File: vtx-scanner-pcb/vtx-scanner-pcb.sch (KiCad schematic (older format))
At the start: 15 parts, among them U1 RX5808, U3 oskj-dc-dc

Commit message: Lots of progress with the schematic and a bit of the PCB
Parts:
- added J2: Conn_01x08_Female, Connector_PinHeader_2.54mm:PinHeader_1x08_P2.54mm_Horizontal, symbol Connector:Conn_01x08_Female
- added R4, R5, R6, R7: 10K, Resistor_SMD:R_1206_3216Metric_Pad1.42x1.75mm_HandSolder, symbol Device:R
- added S1, S2, S3, S4: B3F-1000, digikey-footprints:Switch_Tactile_THT_B3F-1xxx, symbol dk_Tactile-Switches:B3F-1000
- A1: renamed from A?; footprint XCVR_ESP32-WROVER-I -> deets:XCVR_ESP32-WROVER-I
- C1, C2: renamed from C?; footprint (none) -> Capacitor_SMD:CP_Elec_5x5.8
- C3: renamed from C?; footprint (none) -> Capacitor_SMD:C_0805_2012Metric_Pad1.15x1.40mm_HandSolder
- J1: renamed from J?; footprint (none) -> Connector_PinHeader_2.54mm:PinHeader_1x06_P2.54mm_Vertical
- R1, R2: renamed from R?; value 12K -> 10K; footprint (none) -> Resistor_SMD:R_1206_3216Metric_Pad1.42x1.75mm_HandSolder
- R3: renamed from R?; footprint (none) -> Resistor_SMD:R_1206_3216Metric_Pad1.42x1.75mm_HandSolder
- U1: footprint vtx-scanner:RX5808 -> deets:RX5808
- U3: footprint new-joy:oskj-dc-dc -> deets:oskj-dc-dc
- U4: renamed from U?; footprint (none) -> deets:AI-1027-TWT
- gave numbers to parts that had none: 4
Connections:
- net labels added: BUTTON_DOWN, BUTTON_LEFT, BUTTON_RIGHT, BUTTON_UP, SSD1306_CLK, SSD1306_CS, SSD1306_DATA, SSD1306_DC, SSD1306_RST, VRX_CLOCK, VRX_CS, VRX_DATA, VRX_RSSI
- net labels removed: +3V3
- wire segments 33 -> 63
- no-connect marks 6 -> 20
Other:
- note added: "strapping pin\n"
- moved on the sheet: C3, U1

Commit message: Started laying out PCB
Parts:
- removed Q1, Q2, Q3: S8050, Package_TO_SOT_THT:TO-92_Inline, symbol Transistor_BJT:S8050
- removed S1, S2, S3, S4: B3F-1000, digikey-footprints:Switch_Tactile_THT_B3F-1xxx, symbol dk_Tactile-Switches:B3F-1000
- added J3: SMA-J-P-H-RA-TH1, deets:SAMTEC_SMA-J-P-H-RA-TH1, symbol deets:SMA-J-P-H-RA-TH1
- added Q1, Q2, Q3: MMSS8050-H-TP, digikey-footprints:SOT-23-3, symbol dk_Transistors-Bipolar-BJT-Single:MMSS8050-H-TP
- added S1, S2, S3, S4: FSM4JSMATR, deets:Switch_Tactile_SMD_6x6mm, symbol dk_Tactile-Switches:FSM4JSMATR
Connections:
- net labels added: ANT, GNDA
- wire segments 63 -> 64
- no-connect marks 20 -> 19
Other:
- moved on the sheet: R4

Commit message: Fully laid-out 4 layer PCB, the first!
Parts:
- added J4: Conn_01x05, Connector_JST:JST_PH_S5B-PH-K_1x05_P2.00mm_Horizontal, symbol Connector_Generic:Conn_01x05
- added J5: XT60-M, deets:AMASS_XT60-M-SIDE-MOUNT, symbol deets:XT60-M
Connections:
- net +3V3: now also J4.2 (Pin_2)
- net +5V: now also J4.1 (Pin_1)
- net +BATT: now also J5.2 (+)
- net -BATT: now also J3.2 (GND), J3.3 (GND), J3.4 (GND), J3.5 (GND), U1.1 (AGND), U1.3 (AGND), J4.5 (Pin_5), J5.1 (-)
- net GNDA: no longer J3.2 (GND), J3.3 (GND), J3.4 (GND), J3.5 (GND), U1.1 (AGND), U1.3 (AGND)
- net EXP1: now reaches A1.26 (IO4)
- net EXP1: now also J4.3 (Pin_3)
- net EXP2: now reaches A1.7 (IO35)
- net EXP2: now also J4.4 (Pin_4)
- no-connect marks 19 -> 17
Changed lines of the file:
@@
 Text Label 6200 4400 0    50   ~ 0
 BUTTON_DOWN
-NoConn ~ 5000 3300
-NoConn ~ 6200 3900
 NoConn ~ 6200 4700
 Text Label 5000 4100 2    50   ~ 0
@@
 	1    0    0    -1
 $EndComp
-$Comp
-L power:GNDA #PWR0101
-U 1 1 5C8E1232
-P 1600 4050
-F 0 "#PWR0101" H 1600 3800 50  0001 C CNN
-F 1 "GNDA" H 1605 3877 50  0000 C CNN
-F 2 "" H 1600 4050 50  0001 C CNN
-F 3 "" H 1600 4050 50  0001 C CNN
-	1    1600 4050
-	1    0    0    -1
-$EndComp
 Connection ~ 1600 4050
 $Comp
@@
 Wire Wire Line
 	1400 4050 1600 4050
+Text Label 5000 3300 2    50   ~ 0
+EXP1
+Text Label 6200 3900 0    50   ~ 0
+EXP2
+$Comp
+L Connector_Generic:Conn_01x05 J4
+U 1 1 5CB1EFA4
+P 7600 5650
+F 0 "J4" H 7680 5692 50  0000 L CNN
+F 1 "Conn_01x05" H 7680 5601 50  0000 L CNN
+F 2 "Connector_JST:JST_PH_S5B-PH-K_1x05_P2.00mm_Horizontal" H 7600 5650 50  0001 C CNN
+F 3 "~" H 7600 5650 50  0001 C CNN
+	1    7600 5650
+	1    0    0    -1
+$EndComp
+Text Label 7400 5650 2    50   ~ 0
+EXP1
+Text Label 7400 5750 2    50   ~ 0
+EXP2
+$Comp
+L power:GND #PWR024
+U 1 1 5CB1F134
+P 7400 5850
+F 0 "#PWR024" H 7400 5600 50  0001 C CNN
+F 1 "GND" H 7405 5677 50  0000 C CNN
+F 2 "" H 7400 5850 50  0001 C CNN
+F 3 "" H 7400 5850 50  0001 C CNN
+	1    7400 5850
+	1    0    0    -1
+$EndComp
+$Comp
+L power:+5V #PWR023
+U 1 1 5CB1F237
+P 7400 5450
+F 0 "#PWR023" H 7400 5300 50  0001 C CNN
+F 1 "+5V" H 7415 5623 50  0000 C CNN
+F 2 "" H 7400 5450 50  0001 C CNN
+F 3 "" H 7400 5450 50  0001 C CNN
+	1    7400 5450
+	1    0    0    -1
+$EndComp
+Wire Wire Line
+	7400 5550 7250 5550
+Wire Wire Line
+	7250 5550 7250 5450
+$Comp
+L power:+3.3V #PWR01
+U 1 1 5CB204F9
+P 7250 5450
+F 0 "#PWR01" H 7250 5300 50  0001 C CNN
+F 1 "+3.3V" H 7265 5623 50  0000 C CNN
+F 2 "" H 7250 5450 50  0001 C CNN
+F 3 "" H 7250 5450 50  0001 C CNN
+	1    7250 5450
+	1    0    0    -1
+$EndComp
+$Comp
+L deets:XT60-M J5
+U 1 1 5CB22143
+P 3300 1400
+F 0 "J5" H 3194 1033 50  0000 C CNN
+F 1 "XT60-M" H 3194 1124 50  0000 C CNN
+F 2 "deets:AMASS_XT60-M-SIDE-MOUNT" H 3300 1400 50  0001 L BNN
+F 3 "AMASS" H 3300 1400 50  0001 L BNN
+F 4 "None" H 3300 1400 50  0001 L BNN "Field4"
+F 5 "Unavailable" H 3300 1400 50  0001 L BNN "Field6"
+F 6 "Package Analog Devices" H 3300 1400 50  0001 L BNN "Field7"
+F 7 "XT60-M" H 3300 1400 50  0001 L BNN "Field8"
+	1    3300 1400
+	1    0    0    1
+$EndComp
+$Comp
+L power:+BATT #PWR025
+U 1 1 5CB23453
+P 3000 1300
+F 0 "#PWR025" H 3000 1150 50  0001 C CNN
+F 1 "+BATT" H 3015 1473 50  0000 C CNN
+F 2 "" H 3000 1300 50  0001 C CNN
+F 3 "" H 3000 1300 50  0001 C CNN
+	1    3000 1300
+	1    0    0    -1
+$EndComp
+$Comp
+L power:-BATT #PWR026
+U 1 1 5CB23505
+P 3000 1500
+F 0 "#PWR026" H 3000 1350 50  0001 C CNN
+F 1 "-BATT" H 3015 1673 50  0000 C CNN
+F 2 "" H 3000 1500 50  0001 C CNN
+F 3 "" H 3000 1500 50  0001 C CNN
+	1    3000 1500
+	-1   0    0    1
+$EndComp
+$Comp
+L power:GND #PWR?
+U 1 1 5CB24161
+P 1600 4050
+F 0 "#PWR?" H 1600 3800 50  0001 C CNN
+F 1 "GND" H 1605 3877 50  0000 C CNN
+F 2 "" H 1600 4050 50  0001 C CNN
+F 3 "" H 1600 4050 50  0001 C CNN
+	1    1600 4050
+	1    0    0    -1
+$EndComp
 $EndSCHEMATC

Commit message: Continue re-layouting
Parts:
- added CON1: SJ-3523-SMT-TR, deets:Switch_Slide_11.6x4mm_SJ-3523-SMT, symbol dk_Barrel-Audio-Connectors:SJ-3523-SMT-TR
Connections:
- net -BATT: now also CON1.1 (S)
- net VRX_CLOCK: now also A1.14 (IO12); no longer A1.16 (IO13)
- net VRX_DATA: now also A1.16 (IO13); no longer A1.14 (IO12)
- net at U1.10 (AUDIO): now also CON1.3 (R)
- net at U1.11 (VIDEO): now also CON1.2 (T)
- no-connect marks 17 -> 15
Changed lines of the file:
@@
 	2750 4900 2850 4900
 Connection ~ 2750 4350
-NoConn ~ 2700 3950
-NoConn ~ 2700 4050
 Wire Wire Line
 	1700 3850 1600 3850
@@
 Text Label 5000 3700 2    50   ~ 0
 VRX_CS
+Text Label 5000 3500 2    50   ~ 0
+VRX_CLOCK
 Text Label 5000 3600 2    50   ~ 0
-VRX_CLOCK
-Text Label 5000 3500 2    50   ~ 0
 VRX_DATA
 Text Label 5000 4300 2    50   ~ 0
@@
 $EndComp
 $Comp
-L power:GND #PWR?
+L power:GND #PWR027
 U 1 1 5CB24161
 P 1600 4050
-F 0 "#PWR?" H 1600 3800 50  0001 C CNN
+F 0 "#PWR027" H 1600 3800 50  0001 C CNN
 F 1 "GND" H 1605 3877 50  0000 C CNN
 F 2 "" H 1600 4050 50  0001 C CNN
@@
 	1    0    0    -1
 $EndComp
+$Comp
+L dk_Barrel-Audio-Connectors:SJ-3523-SMT-TR CON1
+U 1 1 5CBA07DB
+P 3600 3700
+F 0 "CON1" H 3272 3647 60  0000 R CNN
+F 1 "SJ-3523-SMT-TR" H 3272 3753 60  0000 R CNN
+F 2 "deets:Switch_Slide_11.6x4mm_SJ-3523-SMT" H 3800 3900 60  0001 L CNN
+F 3 "https://www.cui.com/product/resource/digikeypdf/sj-352x-smt_series.pdf" H 3800 4000 60  0001 L CNN
+F 4 "CP-3523SJCT-ND" H 3800 4100 60  0001 L CNN "Digi-Key_PN"
+F 5 "SJ-3523-SMT-TR" H 3800 4200 60  0001 L CNN "MPN"
+F 6 "Connectors, Interconnects" H 3800 4300 60  0001 L CNN "Category"
+F 7 "Barrel - Audio Connectors" H 3800 4400 60  0001 L CNN "Family"
+F 8 "https://www.cui.com/product/resource/digikeypdf/sj-352x-smt_series.pdf" H 3800 4500 60  0001 L CNN "DK_Datasheet_Link"
+F 9 "/product-detail/en/cui-inc/SJ-3523-SMT-TR/CP-3523SJCT-ND/669704" H 3800 4600 60  0001 L CNN "DK_Detail_Page"
+F 10 "CONN JACK STEREO 3.5MM SMD R/A" H 3800 4700 60  0001 L CNN "Description"
+F 11 "CUI Inc." H 3800 4800 60  0001 L CNN "Manufacturer"
+F 12 "Active" H 3800 4900 60  0001 L CNN "Status"
+	1    3600 3700
+	-1   0    0    1
+$EndComp
+Wire Wire Line
+	2750 3850 3000 3850
+Wire Wire Line
+	3000 3850 3000 3600
+Wire Wire Line
+	3000 3600 3200 3600
+Connection ~ 2750 3850
+Wire Wire Line
+	2700 3950 3100 3950
+Wire Wire Line
+	3100 3950 3100 3700
+Wire Wire Line
+	3100 3700 3200 3700
+Wire Wire Line
+	2700 4050 3200 4050
+Wire Wire Line
+	3200 4050 3200 3800
 $EndSCHEMATC

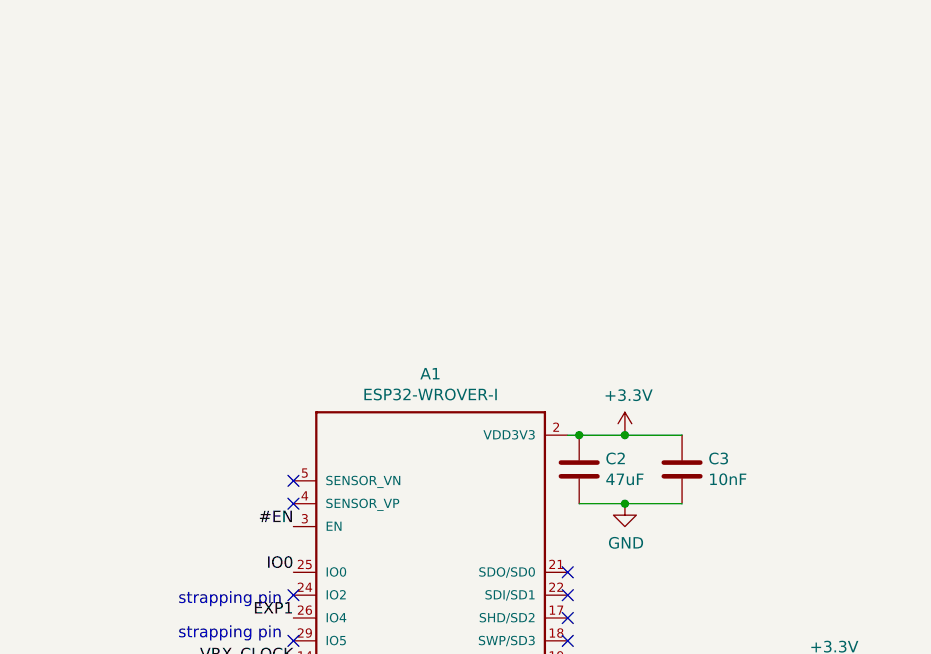
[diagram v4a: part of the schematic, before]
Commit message: Add missing pullups and capacitor for #EN
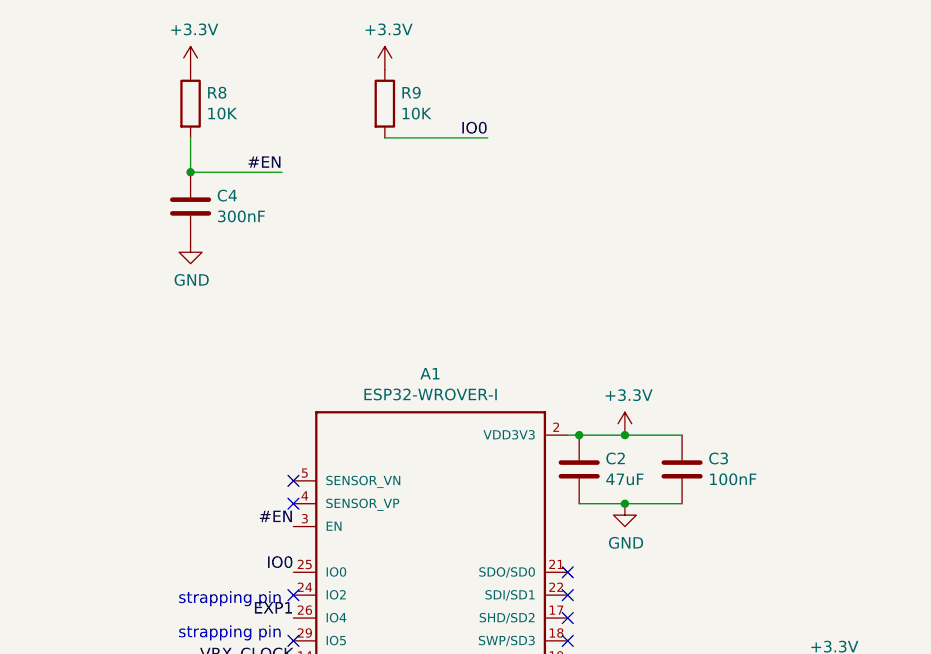
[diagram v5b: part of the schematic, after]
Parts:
- added C4: 300nF, Capacitor_SMD:C_0805_2012Metric_Pad1.15x1.40mm_HandSolder, symbol Device:C
- added R8, R9: 10K, Resistor_SMD:R_1206_3216Metric_Pad1.42x1.75mm_HandSolder, symbol Device:R
- C3: value 10nF -> 100nF
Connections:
- net #EN: now also C4.1, R8.2
- net +3V3: now also R8.1, R9.1
- net -BATT: now also C4.2
- net IO0: now also R9.2
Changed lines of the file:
@@
 Text Label 5000 3100 2    50   ~ 0
 IO0
-Text Label 5000 2900 2    50   ~ 0
+Text Label 4950 1350 2    50   ~ 0
 #EN
 $Comp
@@
 P 6700 2650
 F 0 "C3" H 6815 2696 50  0000 L CNN
-F 1 "10nF" H 6815 2605 50  0000 L CNN
+F 1 "100nF" H 6815 2605 50  0000 L CNN
 F 2 "Capacitor_SMD:C_0805_2012Metric_Pad1.15x1.40mm_HandSolder" H 6738 2500 50  0001 C CNN
 F 3 "~" H 6700 2650 50  0001 C CNN
@@
 Wire Wire Line
 	3200 4050 3200 3800
+Wire Wire Line
+	4950 1350 4550 1350
+Wire Wire Line
+	4550 1350 4550 1200
+$Comp
+L Device:R R8
+U 1 1 5D0E4C72
+P 4550 1050
+F 0 "R8" H 4620 1096 50  0000 L CNN
+F 1 "10K" H 4620 1005 50  0000 L CNN
+F 2 "Resistor_SMD:R_1206_3216Metric_Pad1.42x1.75mm_HandSolder" V 4480 1050 50  0001 C CNN
+F 3 "~" H 4550 1050 50  0001 C CNN
+	1    4550 1050
+	1    0    0    -1
+$EndComp
+$Comp
+L power:+3.3V #PWR0101
+U 1 1 5D0E5144
+P 4550 900
+F 0 "#PWR0101" H 4550 750 50  0001 C CNN
+F 1 "+3.3V" H 4565 1073 50  0000 C CNN
+F 2 "" H 4550 900 50  0001 C CNN
+F 3 "" H 4550 900 50  0001 C CNN
+	1    4550 900
+	1    0    0    -1
+$EndComp
+Text Label 5000 2900 2    50   ~ 0
+#EN
+$Comp
+L Device:C C4
+U 1 1 5D0E76C3
+P 4550 1500
+F 0 "C4" H 4665 1546 50  0000 L CNN
+F 1 "300nF" H 4665 1455 50  0000 L CNN
+F 2 "Capacitor_SMD:C_0805_2012Metric_Pad1.15x1.40mm_HandSolder" H 4588 1350 50  0001 C CNN
+F 3 "~" H 4550 1500 50  0001 C CNN
+	1    4550 1500
+	1    0    0    -1
+$EndComp
+Connection ~ 4550 1350
+$Comp
+L power:GND #PWR0103
+U 1 1 5D0E7B34
+P 4550 1650
+F 0 "#PWR0103" H 4550 1400 50  0001 C CNN
+F 1 "GND" H 4555 1477 50  0000 C CNN
+F 2 "" H 4550 1650 50  0001 C CNN
+F 3 "" H 4550 1650 50  0001 C CNN
+	1    4550 1650
+	1    0    0    -1
+$EndComp
+$Comp
+L Device:R R9
+U 1 1 5D0E975F
+P 5400 1050
+F 0 "R9" H 5470 1096 50  0000 L CNN
+F 1 "10K" H 5470 1005 50  0000 L CNN
+F 2 "Resistor_SMD:R_1206_3216Metric_Pad1.42x1.75mm_HandSolder" V 5330 1050 50  0001 C CNN
+F 3 "~" H 5400 1050 50  0001 C CNN
+	1    5400 1050
+	1    0    0    -1
+$EndComp
+$Comp
+L power:+3.3V #PWR0111
+U 1 1 5D0E9878
+P 5400 900
+F 0 "#PWR0111" H 5400 750 50  0001 C CNN
+F 1 "+3.3V" H 5415 1073 50  0000 C CNN
+F 2 "" H 5400 900 50  0001 C CNN
+F 3 "" H 5400 900 50  0001 C CNN
+	1    5400 900
+	1    0    0    -1
+$EndComp
+Wire Wire Line
+	5400 1200 5850 1200
+Text Label 5850 1200 2    50   ~ 0
+IO0
 $EndSCHEMATC
